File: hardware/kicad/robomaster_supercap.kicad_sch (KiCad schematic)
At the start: 0 parts

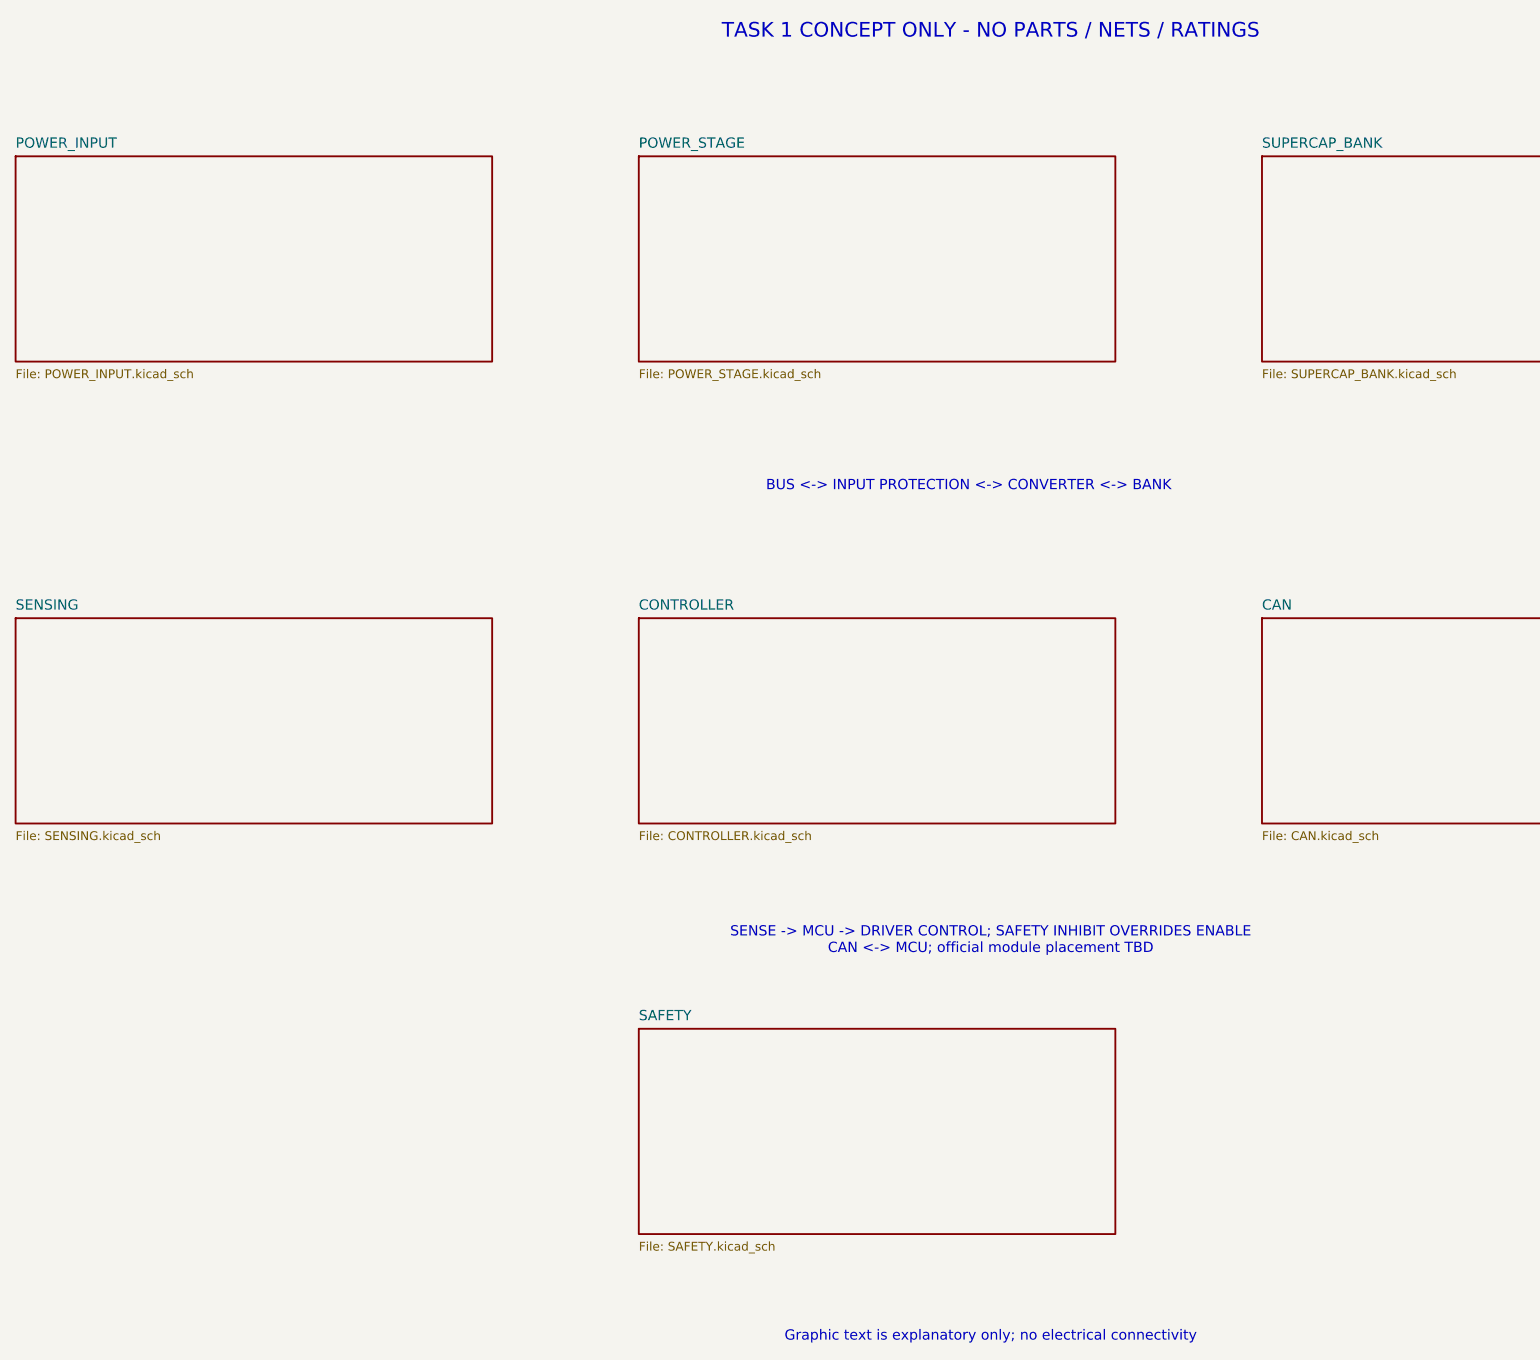
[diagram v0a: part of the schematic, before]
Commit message: hardware: update existing KiCad architecture and add precharge sheet
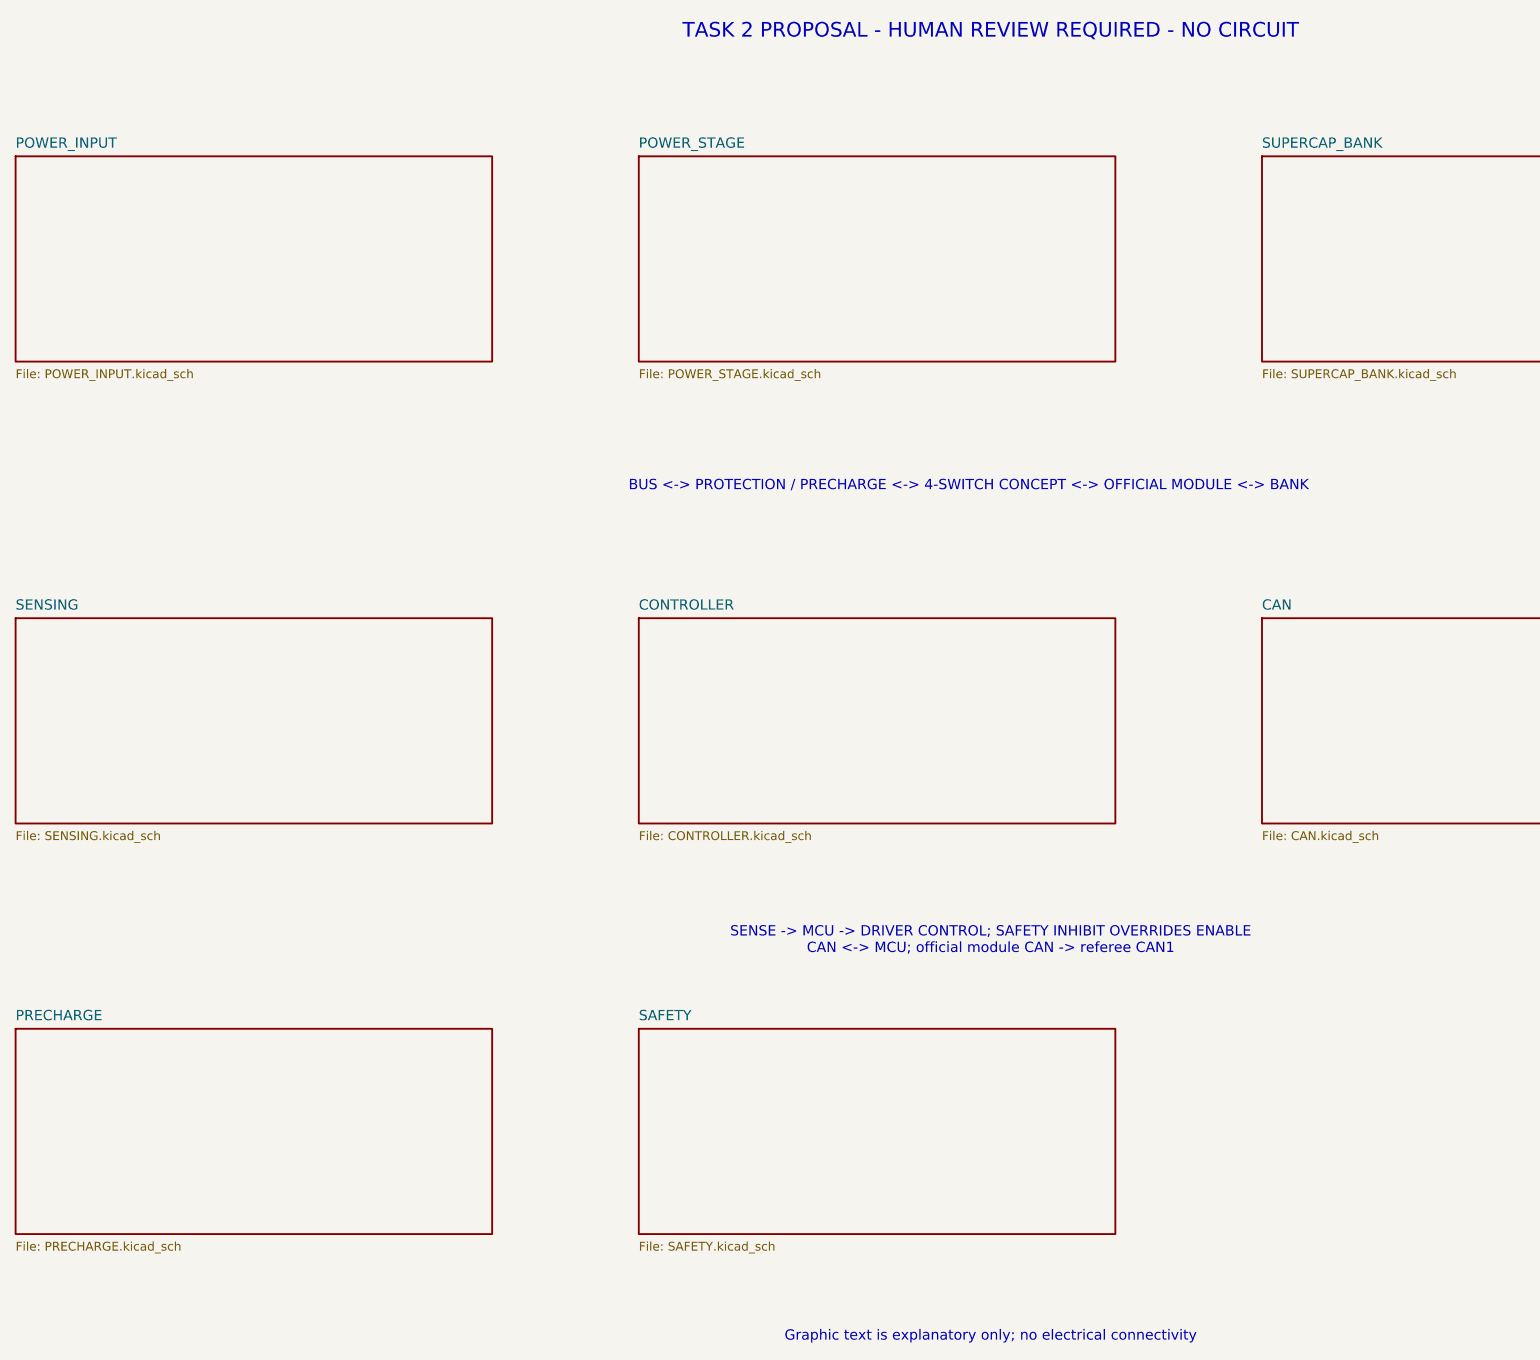
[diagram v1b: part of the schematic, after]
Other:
- added sheet PRECHARGE (PRECHARGE.kicad_sch)
- note added: "BUS <-> PROTECTION / PRECHARGE <-> 4-SWITCH CONCEPT <-> OFFICIAL MODULE <-> BANK"
- note added: "SENSE -> MCU -> DRIVER CONTROL; SAFETY INHIBIT OVERRIDES ENABLE CAN <-> MCU; official module CAN -> referee CAN1"
- note added: "TASK 2 PROPOSAL - HUMAN REVIEW REQUIRED - NO CIRCUIT"
- note removed: "BUS <-> INPUT PROTECTION <-> CONVERTER <-> BANK"
- note removed: "SENSE -> MCU -> DRIVER CONTROL; SAFETY INHIBIT OVERRIDES ENABLE CAN <-> MCU; official module placement TBD"
- note removed: "TASK 1 CONCEPT ONLY - NO PARTS / NETS / RATINGS"

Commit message: hardware: implement prototype Rev A electrical schematic
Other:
- added sheet AUXILIARY_POWER (AUXILIARY_POWER.kicad_sch)
- added sheet CURRENT_SENSING (CURRENT_SENSING.kicad_sch)
- added sheet GATE_DRIVER (GATE_DRIVER.kicad_sch)
- added sheet SAFE_DISCHARGE (SAFE_DISCHARGE.kicad_sch)
- added sheet TEMPERATURE_SENSING (TEMPERATURE_SENSING.kicad_sch)
- added sheet VOLTAGE_SENSING (VOLTAGE_SENSING.kicad_sch)
- note added: "PROTOTYPE REV A SCHEMATIC DRAFT - NOT RELEASED FOR ENERGIZING OR PCB"
- note removed: "BUS <-> PROTECTION / PRECHARGE <-> 4-SWITCH CONCEPT <-> OFFICIAL MODULE <-> BANK"
- note removed: "Graphic text is explanatory only; no electrical connectivity"
- note removed: "SENSE -> MCU -> DRIVER CONTROL; SAFETY INHIBIT OVERRIDES ENABLE CAN <-> MCU; official module CAN -> referee CAN1"
- note removed: "TASK 2 PROPOSAL - HUMAN REVIEW REQUIRED - NO CIRCUIT"
- title: RoboMaster Supercap - Architecture Only -> (none)
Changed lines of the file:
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@@
+(kicad_sch
+  (version 20250114)
+  (generator "eeschema")
+  (paper "A3")
+  (text "PROTOTYPE REV A SCHEMATIC DRAFT - NOT RELEASED FOR ENERGIZING OR PCB" (at 200 15 0) (effects (font (size 2 2))))
+  (sheet
+    (at 20 40)
+    (size 82 40)
+    (stroke (width 0.254) (type default))
+    (fill (color 0 0 0 0))
+    (property "Sheetname" "POWER_INPUT" (at 20 39 0) (effects (font (size 1 1))))
+    (property "Sheetfile" "POWER_INPUT.kicad_sch" (at 20 81 0) (effects (font (size 1 1))))
+    (instances (project "robomaster_supercap" (path "/fe0d835f-f536-483b-a54a-4b6f1f4699ec" (page "2"))))
+  )
+  (sheet
+    (at 115 40)
+    (size 82 40)
+    (stroke (width 0.254) (type default))
+    (fill (color 0 0 0 0))
+    (property "Sheetname" "PRECHARGE" (at 115 39 0) (effects (font (size 1 1))))
+    (property "Sheetfile" "PRECHARGE.kicad_sch" (at 115 81 0) (effects (font (size 1 1))))
+    (instances (project "robomaster_supercap" (path "/fe0d835f-f536-483b-a54a-4b6f1f4699ec" (page "3"))))
+  )
+  (sheet
+    (at 210 40)
+    (size 82 40)
+    (stroke (width 0.254) (type default))
+    (fill (color 0 0 0 0))
+    (property "Sheetname" "POWER_STAGE" (at 210 39 0) (effects (font (size 1 1))))
+    (property "Sheetfile" "POWER_STAGE.kicad_sch" (at 210 81 0) (effects (font (size 1 1))))
+    (instances (project "robomaster_supercap" (path "/fe0d835f-f536-483b-a54a-4b6f1f4699ec" (page "4"))))
+  )
+  (sheet
+    (at 305 40)
+    (size 82 40)
+    (stroke (width 0.254) (type default))
+    (fill (color 0 0 0 0))
+    (property "Sheetname" "GATE_DRIVER" (at 305 39 0) (effects (font (size 1 1))))
+    (property "Sheetfile" "GATE_DRIVER.kicad_sch" (at 305 81 0) (effects (font (size 1 1))))
+    (instances (project "robomaster_supercap" (path "/fe0d835f-f536-483b-a54a-4b6f1f4699ec" (page "5"))))
+  )
+  (sheet
+    (at 20 98)
+    (size 82 40)
+    (stroke (width 0.254) (type default))
+    (fill (color 0 0 0 0))
+    (property "Sheetname" "AUXILIARY_POWER" (at 20 97 0) (effects (font (size 1 1))))
+    (property "Sheetfile" "AUXILIARY_POWER.kicad_sch" (at 20 139 0) (effects (font (size 1 1))))
+    (instances (project "robomaster_supercap" (path "/fe0d835f-f536-483b-a54a-4b6f1f4699ec" (page "6"))))
+  )
+  (sheet
+    (at 115 98)
+    (size 82 40)
+    (stroke (width 0.254) (type default))
+    (fill (color 0 0 0 0))
+    (property "Sheetname" "CONTROLLER" (at 115 97 0) (effects (font (size 1 1))))
+    (property "Sheetfile" "CONTROLLER.kicad_sch" (at 115 139 0) (effects (font (size 1 1))))
+    (instances (project "robomaster_supercap" (path "/fe0d835f-f536-483b-a54a-4b6f1f4699ec" (page "7"))))
+  )
+  (sheet
+    (at 210 98)
+    (size 82 40)
+    (stroke (width 0.254) (type default))
+    (fill (color 0 0 0 0))
+    (property "Sheetname" "CURRENT_SENSING" (at 210 97 0) (effects (font (size 1 1))))
+    (property "Sheetfile" "CURRENT_SENSING.kicad_sch" (at 210 139 0) (effects (font (size 1 1))))
+    (instances (project "robomaster_supercap" (path "/fe0d835f-f536-483b-a54a-4b6f1f4699ec" (page "8"))))
+  )
+  (sheet
+    (at 305 98)
+    (size 82 40)
+    (stroke (width 0.254) (type default))
+    (fill (color 0 0 0 0))
+    (property "Sheetname" "VOLTAGE_SENSING" (at 305 97 0) (effects (font (size 1 1))))
+    (property "Sheetfile" "VOLTAGE_SENSING.kicad_sch" (at 305 139 0) (effects (font (size 1 1))))
+    (instances (project "robomaster_supercap" (path "/fe0d835f-f536-483b-a54a-4b6f1f4699ec" (page "9"))))
+  )
+  (sheet
+    (at 20 156)
+    (size 82 40)
+    (stroke (width 0.254) (type default))
+    (fill (color 0 0 0 0))
+    (property "Sheetname" "TEMPERATURE_SENSING" (at 20 155 0) (effects (font (size 1 1))))
+    (property "Sheetfile" "TEMPERATURE_SENSING.kicad_sch" (at 20 197 0) (effects (font (size 1 1))))
+    (instances (project "robomaster_supercap" (path "/fe0d835f-f536-483b-a54a-4b6f1f4699ec" (page "10"))))
+  )
+  (sheet
+    (at 115 156)
+    (size 82 40)
+    (stroke (width 0.254) (type default))
+    (fill (color 0 0 0 0))
+    (property "Sheetname" "SUPERCAP_BANK" (at 115 155 0) (effects (font (size 1 1))))
+    (property "Sheetfile" "SUPERCAP_BANK.kicad_sch" (at 115 197 0) (effects (font (size 1 1))))
+    (instances (project "robomaster_supercap" (path "/fe0d835f-f536-483b-a54a-4b6f1f4699ec" (page "11"))))
+  )
+  (sheet
+    (at 210 156)
+    (size 82 40)
+    (stroke (width 0.254) (type default))
+    (fill (color 0 0 0 0))
+    (property "Sheetname" "SAFE_DISCHARGE" (at 210 155 0) (effects (font (size 1 1))))
+    (property "Sheetfile" "SAFE_DISCHARGE.kicad_sch" (at 210 197 0) (effects (font (size 1 1))))
+    (instances (project "robomaster_supercap" (path "/fe0d835f-f536-483b-a54a-4b6f1f4699ec" (page "12"))))
+  )
+  (sheet
+    (at 305 156)
+    (size 82 40)
+    (stroke (width 0.254) (type default))
+    (fill (color 0 0 0 0))
+    (property "Sheetname" "CAN" (at 305 155 0) (effects (font (size 1 1))))
+    (property "Sheetfile" "CAN.kicad_sch" (at 305 197 0) (effects (font (size 1 1))))
+    (instances (project "robomaster_supercap" (path "/fe0d835f-f536-483b-a54a-4b6f1f4699ec" (page "13"))))
+  )
+  (sheet
+    (at 20 214)
+    (size 82 40)
+    (stroke (width 0.254) (type default))
+    (fill (color 0 0 0 0))
+    (property "Sheetname" "SAFETY" (at 20 213 0) (effects (font (size 1 1))))
+    (property "Sheetfile" "SAFETY.kicad_sch" (at 20 255 0) (effects (font (size 1 1))))
+    (instances (project "robomaster_supercap" (path "/fe0d835f-f536-483b-a54a-4b6f1f4699ec" (page "14"))))
+  )
+  (sheet
+    (at 115 214)
+    (size 82 40)
+    (stroke (width 0.254) (type default))
+    (fill (color 0 0 0 0))
+    (property "Sheetname" "SENSING" (at 115 213 0) (effects (font (size 1 1))))
+    (property "Sheetfile" "SENSING.kicad_sch" (at 115 255 0) (effects (font (size 1 1))))
+    (instances (project "robomaster_supercap" (path "/fe0d835f-f536-483b-a54a-4b6f1f4699ec" (page "15"))))
+  )
+  (sheet_instances (path "/" (page "1")))
+)
